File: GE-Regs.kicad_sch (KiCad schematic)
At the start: 24 parts, among them J40 Supply, Q40 AO3401A, U40 Switch1SPDT, U50 SY8113BADC, U60 SY8113BADC

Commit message: switched to stm32
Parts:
- removed D40: ZMM5V6, Diode_SMD:D_MiniMELF, symbol Diode:ZMMxx
- removed D41: POWER_LED, LED_SMD:LED_0805_2012Metric, symbol Device:LED
- removed Q40: AO3401A, Package_TO_SOT_SMD:SOT-23, symbol Transistor_FET:AO3401A
- removed R40: 10K, Resistor_SMD:R_0603_1608Metric, symbol Device:R
- removed R41: 1K, Resistor_SMD:R_0603_1608Metric, symbol Device:R
- removed U40: Switch1SPDT, Connector_PinHeader_2.54mm:PinHeader_1x03_P2.54mm_Vertical, symbol NoU265:Switch1SPDT
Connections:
- net VDD: now also J40.2 (Pin_2)
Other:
- moved on the sheet: C40, J40

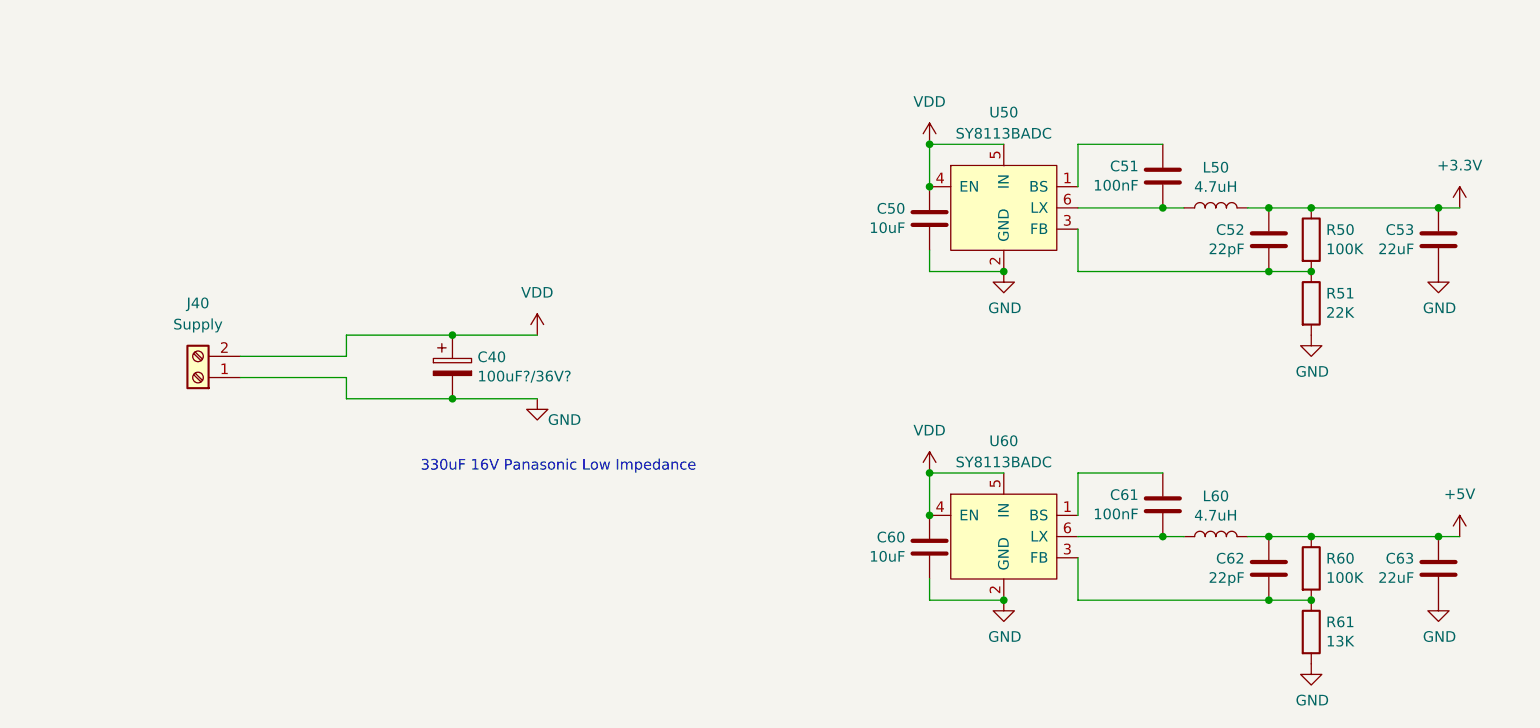
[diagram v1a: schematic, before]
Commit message: moved the Dsub off-board, most of initial layout routed
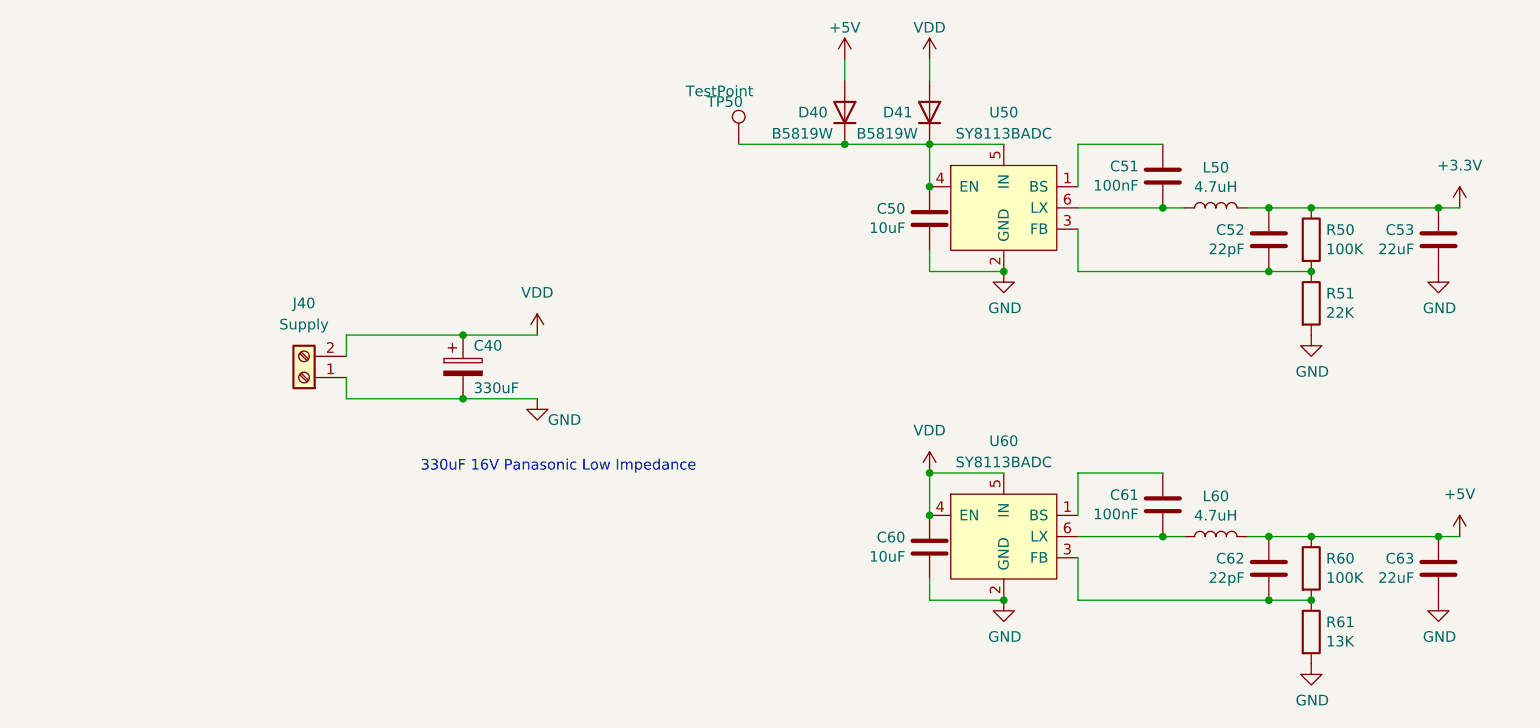
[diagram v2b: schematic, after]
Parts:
- removed C40: 100uF?/36V?, symbol Device:CP
- added C40: 330uF, AlfredoFootprints:TGD_lowESR_cap, symbol Device:C_Polarized
- added D40, D41: B5819W, Diode_SMD:D_SOD-123, symbol Device:D
- added TP50: TestPoint, AlfredoFootprints:GE_TestPoint_Loop, symbol Connector:TestPoint
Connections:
- net +5V: now also D40.2 (A)
- net GND: now also C40.2
- net VDD: now also C40.1, D41.2 (A); no longer C50.2, U50.4 (EN), U50.5 (IN)
- new net: C50.2, D40.1 (K), D41.1 (K), TP50.1, U50.4 (EN), U50.5 (IN)
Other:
- moved on the sheet: J40
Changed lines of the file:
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@@
   (junction (at 205.74 76.2) (diameter 0) (color 0 0 0 0)
   )
-  (junction (at 107.95 83.82) (diameter 0) (color 0 0 0 0)
+  (junction (at 109.22 83.82) (diameter 0) (color 0 0 0 0)
   )
   (junction (at 173.99 76.2) (diameter 0) (color 0 0 0 0)
@@
   (junction (at 193.04 107.95) (diameter 0) (color 0 0 0 0)
   )
+  (junction (at 109.22 91.44) (diameter 0) (color 0 0 0 0)
+  )
+  (junction (at 154.94 60.96) (diameter 0) (color 0 0 0 0)
+  )
+  (junction (at 165.1 60.96) (diameter 0) (color 0 0 0 0)
+  )
   (junction (at 205.74 68.58) (diameter 0) (color 0 0 0 0)
   )
-  (junction (at 165.1 60.96) (diameter 0) (color 0 0 0 0)
-  )
-  (junction (at 107.95 91.44) (diameter 0) (color 0 0 0 0)
-  )
   (junction (at 165.1 105.41) (diameter 0) (color 0 0 0 0)
   )
@@
     (stroke (width 0) (type default) (color 0 0 0 0))
   )
-  (wire (pts (xy 95.25 91.44) (xy 107.95 91.44))
+  (wire (pts (xy 95.25 91.44) (xy 109.22 91.44))
     (stroke (width 0) (type default) (color 0 0 0 0))
   )
@@
     (stroke (width 0) (type default) (color 0 0 0 0))
   )
-  (wire (pts (xy 95.25 83.82) (xy 107.95 83.82))
-    (stroke (width 0) (type default) (color 0 0 0 0))
-  )
-  (wire (pts (xy 107.95 83.82) (xy 118.11 83.82))
+  (wire (pts (xy 109.22 91.44) (xy 118.11 91.44))
+    (stroke (width 0) (type default) (color 0 0 0 0))
+  )
+  (wire (pts (xy 142.24 60.96) (xy 154.94 60.96))
+    (stroke (width 0) (type default) (color 0 0 0 0))
+  )
+  (wire (pts (xy 95.25 83.82) (xy 109.22 83.82))
     (stroke (width 0) (type default) (color 0 0 0 0))
   )
@@
     (stroke (width 0) (type default) (color 0 0 0 0))
   )
+  (wire (pts (xy 154.94 60.96) (xy 165.1 60.96))
+    (stroke (width 0) (type default) (color 0 0 0 0))
+  )
   (wire (pts (xy 182.88 100.33) (xy 193.04 100.33))
     (stroke (width 0) (type default) (color 0 0 0 0))
   )
+  (wire (pts (xy 109.22 83.82) (xy 118.11 83.82))
+    (stroke (width 0) (type default) (color 0 0 0 0))
+  )
   (wire (pts (xy 182.88 115.57) (xy 205.74 115.57))
     (stroke (width 0) (type default) (color 0 0 0 0))
@@
     (stroke (width 0) (type default) (color 0 0 0 0))
   )
+  (wire (pts (xy 154.94 50.8) (xy 154.94 53.34))
+    (stroke (width 0) (type default) (color 0 0 0 0))
+  )
   (wire (pts (xy 182.88 107.95) (xy 193.04 107.95))
     (stroke (width 0) (type default) (color 0 0 0 0))
@@
     (stroke (width 0) (type default) (color 0 0 0 0))
   )
-  (wire (pts (xy 107.95 91.44) (xy 118.11 91.44))
-    (stroke (width 0) (type default) (color 0 0 0 0))
-  )
   (wire (pts (xy 182.88 76.2) (xy 205.74 76.2))
     (stroke (width 0) (type default) (color 0 0 0 0))
@@
     (stroke (width 0) (type default) (color 0 0 0 0))
   )
+  (wire (pts (xy 165.1 50.8) (xy 165.1 53.34))
+    (stroke (width 0) (type default) (color 0 0 0 0))
+  )
   (wire (pts (xy 226.06 107.95) (xy 228.6 107.95))
     (stroke (width 0) (type default) (color 0 0 0 0))
@@
     (stroke (width 0) (type default) (color 0 0 0 0))
   )
-  (wire (pts (xy 82.55 88.9) (xy 95.25 88.9))
-    (stroke (width 0) (type default) (color 0 0 0 0))
-  )
   (wire (pts (xy 226.06 68.58) (xy 228.6 68.58))
     (stroke (width 0) (type default) (color 0 0 0 0))
@@
   )
   (wire (pts (xy 210.82 68.58) (xy 226.06 68.58))
-    (stroke (width 0) (type default) (color 0 0 0 0))
-  )
-  (wire (pts (xy 82.55 86.36) (xy 95.25 86.36))
     (stroke (width 0) (type default) (color 0 0 0 0))
   )
@@
     (pin "1")
   )
-  (symbol (lib_id "Connector:Screw_Terminal_01x02") (at 77.47 88.9 180) (unit 1)
+  (symbol (lib_id "Connector:Screw_Terminal_01x02") (at 90.17 88.9 180) (unit 1)
     (in_bom yes) (on_board yes) (fields_autoplaced)
-    (property "Reference" "J40" (id 0) (at 77.47 80.01 0))
-    (property "Value" "Supply" (id 1) (at 77.47 82.55 0))
-    (property "Footprint" "TerminalBlock:TerminalBlock_bornier-2_P5.08mm" (id 2) (at 77.47 88.9 0)
-      (effects (font (size 1.27 1.27)) hide)
-    )
-    (property "Datasheet" "" (id 3) (at 77.47 88.9 0)
+    (property "Reference" "J40" (id 0) (at 90.17 80.01 0))
+    (property "Value" "Supply" (id 1) (at 90.17 82.55 0))
+    (property "Footprint" "TerminalBlock:TerminalBlock_bornier-2_P5.08mm" (id 2) (at 90.17 88.9 0)
+      (effects (font (size 1.27 1.27)) hide)
+    )
+    (property "Datasheet" "~" (id 3) (at 90.17 88.9 0)
+      (effects (font (size 1.27 1.27)) hide)
+    )
+    (property "LCSC" "~" (id 4) (at 90.17 88.9 0)
+      (effects (font (size 1.27 1.27)) hide)
+    )
+    (pin "1")
+    (pin "2")
+  )
+  (symbol (lib_id "power:+5V") (at 154.94 50.8 0) (unit 1)
+    (in_bom yes) (on_board yes)
+    (property "Reference" "#PWR0161" (id 0) (at 154.94 54.61 0)
+      (effects (font (size 1.27 1.27)) hide)
+    )
+    (property "Value" "+5V" (id 1) (at 154.94 46.99 0))
+    (property "Footprint" "" (id 2) (at 154.94 50.8 0)
+      (effects (font (size 1.27 1.27)) hide)
+    )
+    (property "Datasheet" "" (id 3) (at 154.94 50.8 0)
+      (effects (font (size 1.27 1.27)) hide)
+    )
+    (pin "1")
+  )
+  (symbol (lib_id "Device:D") (at 154.94 57.15 270) (mirror x) (unit 1)
+    (in_bom yes) (on_board yes)
+    (property "Reference" "D40" (id 0) (at 151.13 57.15 90))
+    (property "Value" "B5819W" (id 1) (at 149.86 59.69 90))
+    (property "Footprint" "Diode_SMD:D_SOD-123" (id 2) (at 154.94 57.15 0)
+      (effects (font (size 1.27 1.27)) hide)
+    )
+    (property "Datasheet" "?" (id 3) (at 154.94 57.15 0)
+      (effects (font (size 1.27 1.27)) hide)
+    )
+    (property "LCSC" "C8598" (id 4) (at 154.94 57.15 0)
+      (effects (font (size 1.27 1.27)) hide)
+    )
+    (pin "1")
+    (pin "2")
+  )
+  (symbol (lib_id "Device:D") (at 165.1 57.15 270) (mirror x) (unit 1)
+    (in_bom yes) (on_board yes)
+    (property "Reference" "D41" (id 0) (at 161.29 57.15 90))
+    (property "Value" "B5819W" (id 1) (at 160.02 59.69 90))
+    (property "Footprint" "Diode_SMD:D_SOD-123" (id 2) (at 165.1 57.15 0)
+      (effects (font (size 1.27 1.27)) hide)
+    )
+    (property "Datasheet" "?" (id 3) (at 165.1 57.15 0)
+      (effects (font (size 1.27 1.27)) hide)
+    )
+    (property "LCSC" "C8598" (id 4) (at 165.1 57.15 0)
       (effects (font (size 1.27 1.27)) hide)
     )
@@
     (pin "1")
   )
+  (symbol (lib_id "Connector:TestPoint") (at 142.24 60.96 0) (unit 1)
+    (in_bom yes) (on_board yes)
+    (property "Reference" "TP50" (id 0) (at 138.43 55.88 0)
+      (effects (font (size 1.27 1.27)) (justify left))
+    )
+    (property "Value" "TestPoint" (id 1) (at 135.89 54.61 0)
+      (effects (font (size 1.27 1.27)) (justify left))
+    )
+    (property "Footprint" "AlfredoFootprints:GE_TestPoint_Loop" (id 2) (at 147.32 60.96 0)
+      (effects (font (size 1.27 1.27)) hide)
+    )
+    (property "Datasheet" "~" (id 3) (at 147.32 60.96 0)
+      (effects (font (size 1.27 1.27)) hide)
+    )
+    (pin "1")
+  )
   (symbol (lib_id "power:+3.3V") (at 228.6 68.58 0) (unit 1)
     (in_bom yes) (on_board yes) (fields_autoplaced)
@@
     (pin "1")
   )
-  (symbol (lib_id "Device:CP") (at 107.95 87.63 0) (unit 1)
-    (in_bom yes) (on_board yes)
-    (property "Reference" "C40" (id 0) (at 110.9472 86.4616 0)
-      (effects (font (size 1.27 1.27)) (justify left))
-    )
-    (property "Value" "100uF?/36V?" (id 1) (at 110.9472 88.773 0)
-      (effects (font (size 1.27 1.27)) (justify left))
-    )
-    (property "Footprint" "" (id 2) (at 108.9152 91.44 0)
-      (effects (font (size 1.27 1.27)) hide)
-    )
-    (property "Datasheet" "" (id 3) (at 107.95 87.63 0)
-      (effects (font (size 1.27 1.27)) hide)
-    )
-    (property "LCSC" "" (id 4) (at 107.95 87.63 0)
-      (effects (font (size 1.27 1.27)) hide)
-    )
-    (pin "1")
-    (pin "2")
-  )
-  (symbol (lib_id "power:VDD") (at 165.1 60.96 0) (unit 1)
-    (in_bom yes) (on_board yes) (fields_autoplaced)
-    (property "Reference" "#PWR0132" (id 0) (at 165.1 64.77 0)
-      (effects (font (size 1.27 1.27)) hide)
-    )
-    (property "Value" "VDD" (id 1) (at 165.1 55.88 0))
-    (property "Footprint" "" (id 2) (at 165.1 60.96 0)
-      (effects (font (size 1.27 1.27)) hide)
-    )
-    (property "Datasheet" "" (id 3) (at 165.1 60.96 0)
-      (effects (font (size 1.27 1.27)) hide)
-    )
+  (symbol (lib_id "Device:C_Polarized") (at 109.22 87.63 0) (unit 1)
+    (in_bom yes) (on_board yes)
+    (property "Reference" "C40" (id 0) (at 110.49 85.09 0)
+      (effects (font (size 1.27 1.27)) (justify left))
+    )
+    (property "Value" "330uF" (id 1) (at 110.49 90.17 0)
+      (effects (font (size 1.27 1.27)) (justify left))
+    )
+    (property "Footprint" "AlfredoFootprints:TGD_lowESR_cap" (id 2) (at 110.1852 91.44 0)
+      (effects (font (size 1.27 1.27)) hide)
+    )
+    (property "Datasheet" "~" (id 3) (at 109.22 87.63 0)
+      (effects (font (size 1.27 1.27)) hide)
+    )
+    (property "LCSC" "~" (id 4) (at 109.22 87.63 0)
+      (effects (font (size 1.27 1.27)) hide)
+    )
+    (pin "1")
+    (pin "2")
+  )
+  (symbol (lib_id "power:VDD") (at 165.1 50.8 0) (unit 1)
+    (in_bom yes) (on_board yes)
+    (property "Reference" "#PWR0162" (id 0) (at 165.1 54.61 0)
+      (effects (font (size 1.27 1.27)) hide)
+    )
+    (property "Value" "VDD" (id 1) (at 165.1 46.99 0))
+    (property "Footprint" "" (id 2) (at 165.1 50.8 0)
+      (effects (font (size 1.27 1.27)) hide)
+    )
+    (property "Datasheet" "" (id 3) (at 165.1 50.8 0)
+      (effects (font (size 1.27 1.27)) hide)
+    )

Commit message: Updated BOM
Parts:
- C50, C60: LCSC C15850 -> C2922482
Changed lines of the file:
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@@
       (effects (font (size 1.27 1.27)) hide)
     )
-    (property "Datasheet" "https://lcsc.com/product-detail/Multilayer-Ceramic-Capacitors-MLCC-SMD-SMT_Samsung-Electro-Mechanics-CL21A106KAYNNNE_C15850.html" (id 3) (at 165.1 109.22 0)
-      (effects (font (size 1.27 1.27)) hide)
-    )
-    (property "LCSC" "C15850" (id 4) (at 165.1 109.22 0)
+    (property "Datasheet" "https://lcsc.com/product-detail/Multilayer-Ceramic-Capacitors-MLCC-SMD-SMT_Samsung-Electro-Mechanics-CL10A106MA8NRNC_C2922482.html" (id 3) (at 165.1 109.22 0)
+      (effects (font (size 1.27 1.27)) hide)
+    )
+    (property "LCSC" "C2922482" (id 4) (at 165.1 109.22 0)
       (effects (font (size 1.27 1.27)) hide)
     )
@@
       (effects (font (size 1.27 1.27)) hide)
     )
-    (property "Datasheet" "https://lcsc.com/product-detail/Multilayer-Ceramic-Capacitors-MLCC-SMD-SMT_Samsung-Electro-Mechanics-CL21A106KAYNNNE_C15850.html" (id 3) (at 165.1 69.85 0)
-      (effects (font (size 1.27 1.27)) hide)
-    )
-    (property "LCSC" "C15850" (id 4) (at 165.1 69.85 0)
+    (property "Datasheet" "https://lcsc.com/product-detail/Multilayer-Ceramic-Capacitors-MLCC-SMD-SMT_Samsung-Electro-Mechanics-CL10A106MA8NRNC_C2922482.html" (id 3) (at 165.1 69.85 0)
+      (effects (font (size 1.27 1.27)) hide)
+    )
+    (property "LCSC" "C2922482" (id 4) (at 165.1 69.85 0)
       (effects (font (size 1.27 1.27)) hide)
     )
@@
       (effects (font (size 1.27 1.27)) hide)
     )
-    (property "Datasheet" "?" (id 3) (at 154.94 57.15 0)
+    (property "Datasheet" "https://lcsc.com/product-detail/Schottky-Barrier-Diodes-SBD_Jiangsu-Changjing-Electronics-Technology-Co-Ltd-B5819W-SL_C8598.html" (id 3) (at 154.94 57.15 0)
       (effects (font (size 1.27 1.27)) hide)
     )
@@
       (effects (font (size 1.27 1.27)) hide)
     )
-    (property "Datasheet" "?" (id 3) (at 165.1 57.15 0)
+    (property "Datasheet" "https://lcsc.com/product-detail/Schottky-Barrier-Diodes-SBD_Jiangsu-Changjing-Electronics-Technology-Co-Ltd-B5819W-SL_C8598.html" (id 3) (at 165.1 57.15 0)
       (effects (font (size 1.27 1.27)) hide)
     )
@@
       (effects (font (size 1.27 1.27)) hide)
     )
+    (property "LCSC" "~" (id 4) (at 142.24 60.96 0)
+      (effects (font (size 1.27 1.27)) hide)
+    )

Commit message: major schematic and pcb changes for production ready prototype
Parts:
- removed C51: 100nF, Capacitor_SMD:C_0603_1608Metric, symbol Device:C
- removed D40, D41: B5819W, Diode_SMD:D_SOD-123, symbol Device:D
- removed J40: Supply, TerminalBlock:TerminalBlock_bornier-2_P5.08mm, symbol Connector:Screw_Terminal_01x02
- removed L50: 4.7uH, Inductor_SMD:L_1210_3225Metric, symbol Device:L
- removed R50: 100K, Resistor_SMD:R_0603_1608Metric, symbol Device:R
- removed R51: 22K, Resistor_SMD:R_0603_1608Metric, symbol Device:R
- removed TP50: TestPoint, AlfredoFootprints:GE_TestPoint_Loop, symbol Connector:TestPoint
- removed U50: SY8113BADC, Package_TO_SOT_SMD:TSOT-23-6, symbol NoU265:SY8113BADC
- added C41: 330uF, AlfredoFootprints:Cap_THT_LowESR_330uF, symbol Device:C_Polarized
- added J40: Vin, AlfredoFootprints:GE_PwrPad1, symbol Connector_Generic:Conn_01x01
- added J41: Gnd, AlfredoFootprints:GE_PwrPad1, symbol Connector_Generic:Conn_01x01
- added TP60: TestPoint, AlfredoFootprints:GE_TestPoint_Loop, symbol Connector:TestPoint
- added U50: SPX3819M5-L-3-3, Package_TO_SOT_SMD:SOT-23-5, symbol Regulator_Linear:SPX3819M5-L-3-3
- C40: footprint AlfredoFootprints:TGD_lowESR_cap -> AlfredoFootprints:Cap_THT_LowESR_330uF
- C50, C60: value 10uF -> 2.2uF, 50V; LCSC C2922482 -> C913904
- C52: value 22pF -> 10nF, 6.3V; footprint Capacitor_SMD:C_0603_1608Metric -> Capacitor_SMD:C_0402_1005Metric; LCSC C1653 -> C15195
- C53: value 22uF -> 2.2uF, 6.3V; footprint Capacitor_SMD:C_0603_1608Metric -> Capacitor_SMD:C_0402_1005Metric; LCSC C59461 -> C12530
- C61: footprint Capacitor_SMD:C_0603_1608Metric -> Capacitor_SMD:C_0402_1005Metric; LCSC C14663 -> C307331
- C62: footprint Capacitor_SMD:C_0603_1608Metric -> Capacitor_SMD:C_0402_1005Metric; LCSC C1653 -> C1555
- C63: value 22uF -> 22uF, 10V; footprint Capacitor_SMD:C_0603_1608Metric -> Capacitor_SMD:C_0402_1005Metric; LCSC C59461 -> C77002
- R60: footprint Resistor_SMD:R_0603_1608Metric -> Resistor_SMD:R_0402_1005Metric; LCSC C25803 -> (none)
- R61: footprint Resistor_SMD:R_0603_1608Metric -> Resistor_SMD:R_0402_1005Metric; LCSC C22797 -> (none)
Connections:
- net +3V3: now also U50.5 (OUT); no longer C52.2
- net +5V: now also C50.2, TP60.1, U50.1 (IN), U50.3 (EN)
- net GND: now also C52.1, C41.2, J41.1 (Pin_1), U50.2 (GND)
- net VDD: now also C41.1, J40.1 (Pin_1)
- new net: C52.2, U50.4 (BP)

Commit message: First rev of layout before routing
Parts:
- removed C50: 2.2uF, 50V, Capacitor_SMD:C_0603_1608Metric, symbol Device:C
- U50: LCSC (none) -> C9055
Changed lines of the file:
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@@
   (junction (at 165.1 105.41) (diameter 0) (color 0 0 0 0)
   )
-  (junction (at 168.91 67.31) (diameter 0) (color 0 0 0 0)
-  )
   (junction (at 210.82 107.95) (diameter 0) (color 0 0 0 0)
   )
@@
   (junction (at 210.82 115.57) (diameter 0) (color 0 0 0 0)
   )
-  (junction (at 185.42 77.47) (diameter 0) (color 0 0 0 0)
-  )
   (junction (at 218.44 107.95) (diameter 0) (color 0 0 0 0)
   )
@@
     (stroke (width 0) (type default) (color 0 0 0 0))
   )
-  (wire (pts (xy 168.91 74.93) (xy 168.91 77.47))
-    (stroke (width 0) (type default) (color 0 0 0 0))
-  )
   (wire (pts (xy 175.26 69.85) (xy 175.26 67.31))
     (stroke (width 0) (type default) (color 0 0 0 0))
@@
     (stroke (width 0) (type default) (color 0 0 0 0))
   )
-  (wire (pts (xy 168.91 77.47) (xy 185.42 77.47))
-    (stroke (width 0) (type default) (color 0 0 0 0))
-  )
   (wire (pts (xy 182.88 105.41) (xy 182.88 100.33))
     (stroke (width 0) (type default) (color 0 0 0 0))
@@
     (stroke (width 0) (type default) (color 0 0 0 0))
   )
-  (wire (pts (xy 165.1 67.31) (xy 168.91 67.31))
-    (stroke (width 0) (type default) (color 0 0 0 0))
-  )
   (wire (pts (xy 205.74 115.57) (xy 210.82 115.57))
     (stroke (width 0) (type default) (color 0 0 0 0))
@@
     (stroke (width 0) (type default) (color 0 0 0 0))
   )
-  (wire (pts (xy 168.91 67.31) (xy 175.26 67.31))
+  (wire (pts (xy 165.1 67.31) (xy 175.26 67.31))
     (stroke (width 0) (type default) (color 0 0 0 0))
   )
@@
       (effects (font (size 1.27 1.27)) hide)
     )
+    (property "LCSC" "C9055" (id 4) (at 185.42 69.85 0)
+      (effects (font (size 1.27 1.27)) hide)
+    )
     (pin "1")
     (pin "2")
@@
     (pin "5")
   )
-  (symbol (lib_id "Device:C") (at 168.91 71.12 0) (mirror x) (unit 1)
-    (in_bom yes) (on_board yes)
-    (property "Reference" "C50" (id 0) (at 166.0144 69.9516 0)
-      (effects (font (size 1.27 1.27)) (justify right))
-    )
-    (property "Value" "2.2uF, 50V" (id 1) (at 166.0144 72.263 0)
-      (effects (font (size 1.27 1.27)) (justify right))
-    )
-    (property "Footprint" "Capacitor_SMD:C_0603_1608Metric" (id 2) (at 169.8752 67.31 0)
-      (effects (font (size 1.27 1.27)) hide)
-    )
-    (property "Datasheet" "https://lcsc.com/product-detail/Multilayer-Ceramic-Capacitors-MLCC---SMD-SMT_Samsung-Electro-Mechanics-Samsung-Electro-Mechanics-CL10A225KB8NNNC_C913904.html" (id 3) (at 168.91 71.12 0)
-      (effects (font (size 1.27 1.27)) hide)
-    )
-    (property "LCSC" "C913904" (id 4) (at 168.91 71.12 0)
-      (effects (font (size 1.27 1.27)) hide)
-    )
-    (pin "1")
-    (pin "2")
-  )
 )
